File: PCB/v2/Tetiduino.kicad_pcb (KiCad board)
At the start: 2 copper layers, 53.3 x 57.8 mm, 37 parts, among them J1 Conn_01x08_Male, J2 Conn_01x06_Male, J3 Conn_01x10_Male, J4 Conn_01x07_Male, J5 AVR-ISP-6, J6 Conn_01x06_Male, SW1 SW_Push, U1 ATmega328-P, U2 LM358, U3 AMS1117-3.3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

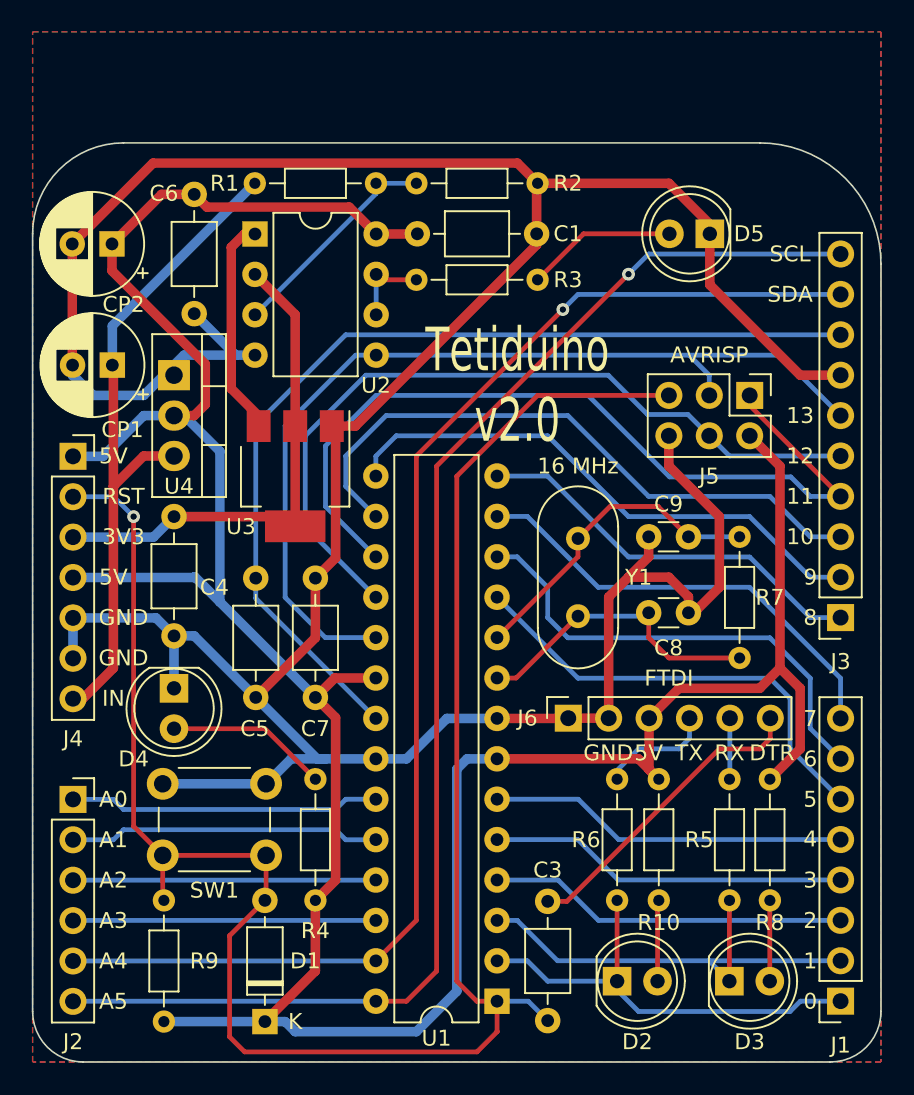
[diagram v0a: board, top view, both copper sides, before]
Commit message: Fixed PCBs for production.
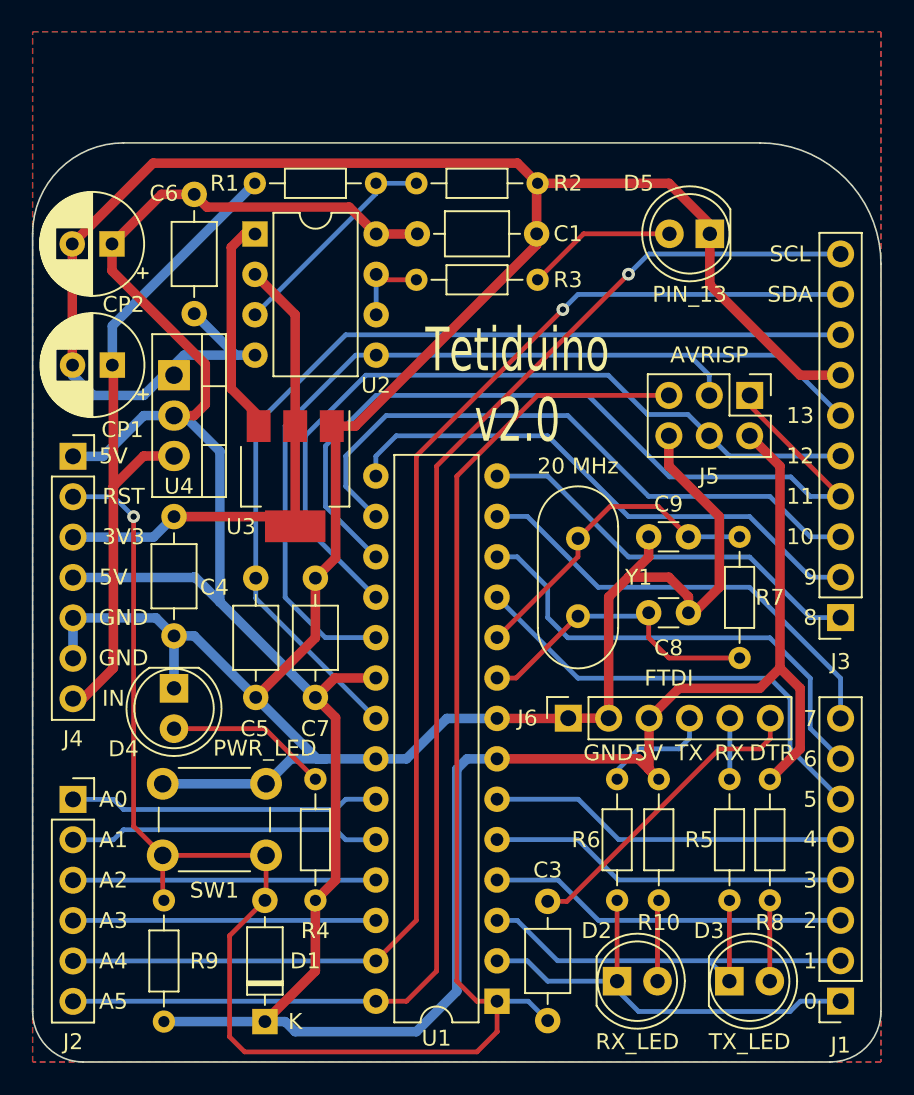
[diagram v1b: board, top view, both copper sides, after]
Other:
- board text added: "20 MHz"
- board text added: "PIN_13"
- board text added: "PWR_LED"
- board text added: "RX_LED"
- board text added: "TX_LED"
- board text removed: "16 MHz"
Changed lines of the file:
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@@
     (property "Sheetname" "")
     (attr through_hole)
-    (fp_text reference "D5" (at -2.465 0) (layer "F.SilkS")
+    (fp_text reference "D5" (at 4.48 3.175) (layer "F.SilkS")
       (effects (font (size 1 1) (thickness 0.15)))
     )
@@
     (property "Sheetname" "")
     (attr through_hole)
-    (fp_text reference "D3" (at 1.27 3.81) (layer "F.SilkS")
+    (fp_text reference "D3" (at -1.29 -3.175) (layer "F.SilkS")
       (effects (font (size 1 1) (thickness 0.15)))
     )
@@
     (property "Sheetname" "")
     (attr through_hole)
-    (fp_text reference "D2" (at 1.27 3.81) (layer "F.SilkS")
+    (fp_text reference "D2" (at -1.29 -3.175) (layer "F.SilkS")
       (effects (font (size 1 1) (thickness 0.15)))
     )
@@
     (property "Sheetname" "")
     (attr through_hole)
-    (fp_text reference "D4" (at 4.445 2.54 -180) (layer "F.SilkS")
+    (fp_text reference "D4" (at 3.81 3.175 -180) (layer "F.SilkS")
       (effects (font (size 1 1) (thickness 0.15)))
     )
@@
     (effects (font (size 1 1) (thickness 0.15)))
   )
+  (gr_text "PWR_LED" (at 136.525 120.61) (layer "F.SilkS")
+    (effects (font (size 1 1) (thickness 0.15)))
+  )
   (gr_text "DTR" (at 168.402 120.904) (layer "F.SilkS")
     (effects (font (size 1 1) (thickness 0.15)))
@@
     (effects (font (size 1 1) (thickness 0.15)))
   )
-  (gr_text "16 MHz" (at 156.21 102.87) (layer "F.SilkS")
+  (gr_text "20 MHz" (at 156.21 102.87) (layer "F.SilkS")
     (effects (font (size 1 1) (thickness 0.15)))
   )
@@
     (effects (font (size 1 1) (thickness 0.15)))
   )
+  (gr_text "PIN_13" (at 163.23 92.075) (layer "F.SilkS")
+    (effects (font (size 1 1) (thickness 0.15)))
+  )
   (gr_text "FTDI" (at 161.925 116.205) (layer "F.SilkS")
     (effects (font (size 1 1) (thickness 0.15)))
@@
     (effects (font (size 1 1) (thickness 0.15)))
   )
+  (gr_text "TX_LED" (at 167 139.065) (layer "F.SilkS")
+    (effects (font (size 1 1) (thickness 0.15)))
+  )
   (gr_text "1" (at 170.815 133.985) (layer "F.SilkS")
     (effects (font (size 1 1) (thickness 0.15)))
   )
+  (gr_text "RX_LED" (at 159.94 139.065) (layer "F.SilkS")
+    (effects (font (size 1 1) (thickness 0.15)))
+  )
